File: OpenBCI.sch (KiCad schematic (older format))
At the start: 12 parts, among them U6 ADS1299

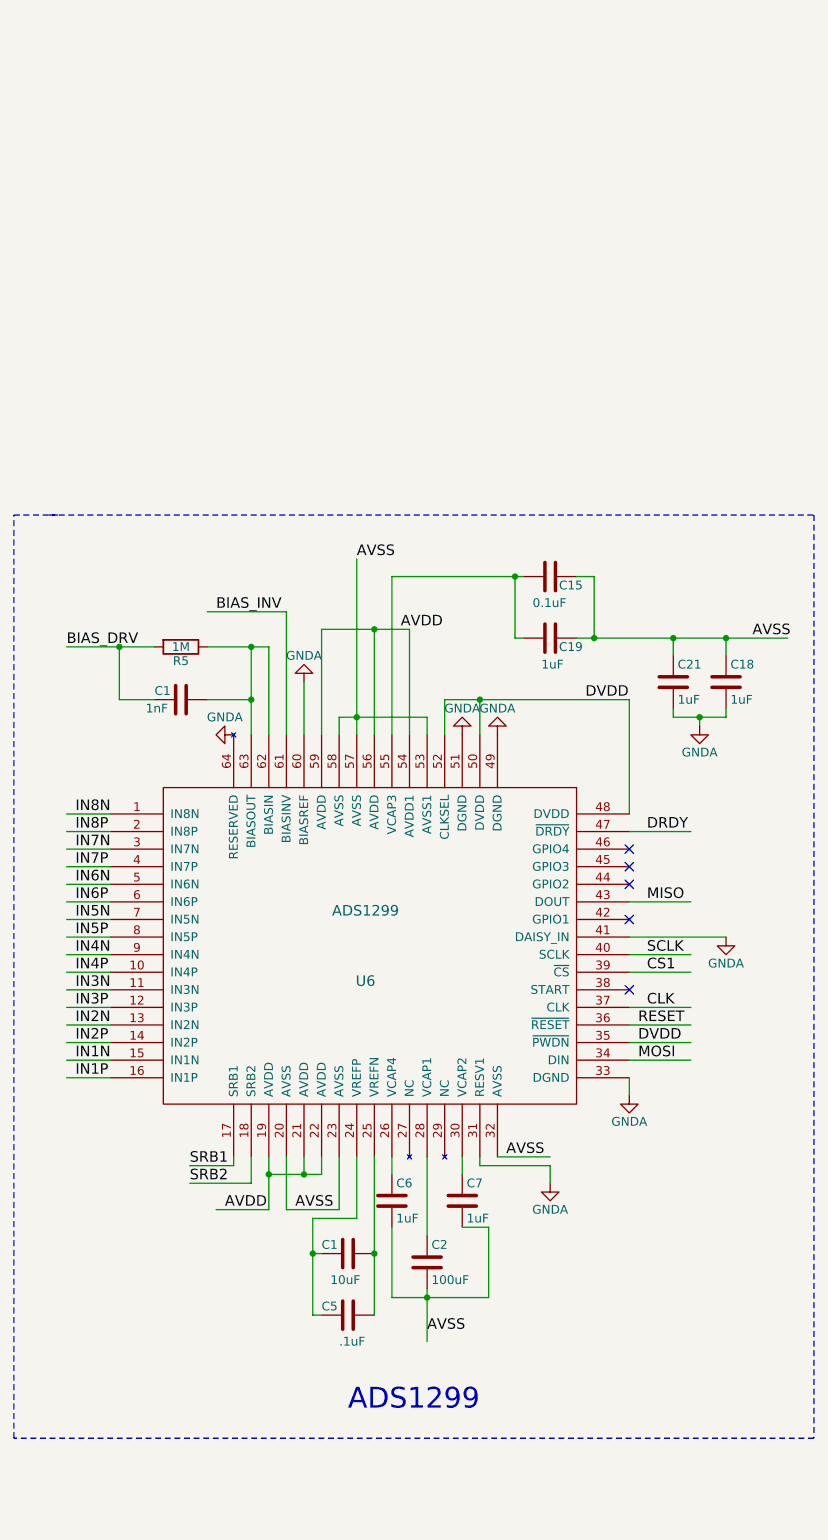
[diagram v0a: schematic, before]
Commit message: Chipkit pin breakout, input connector and daisy bus blocks added
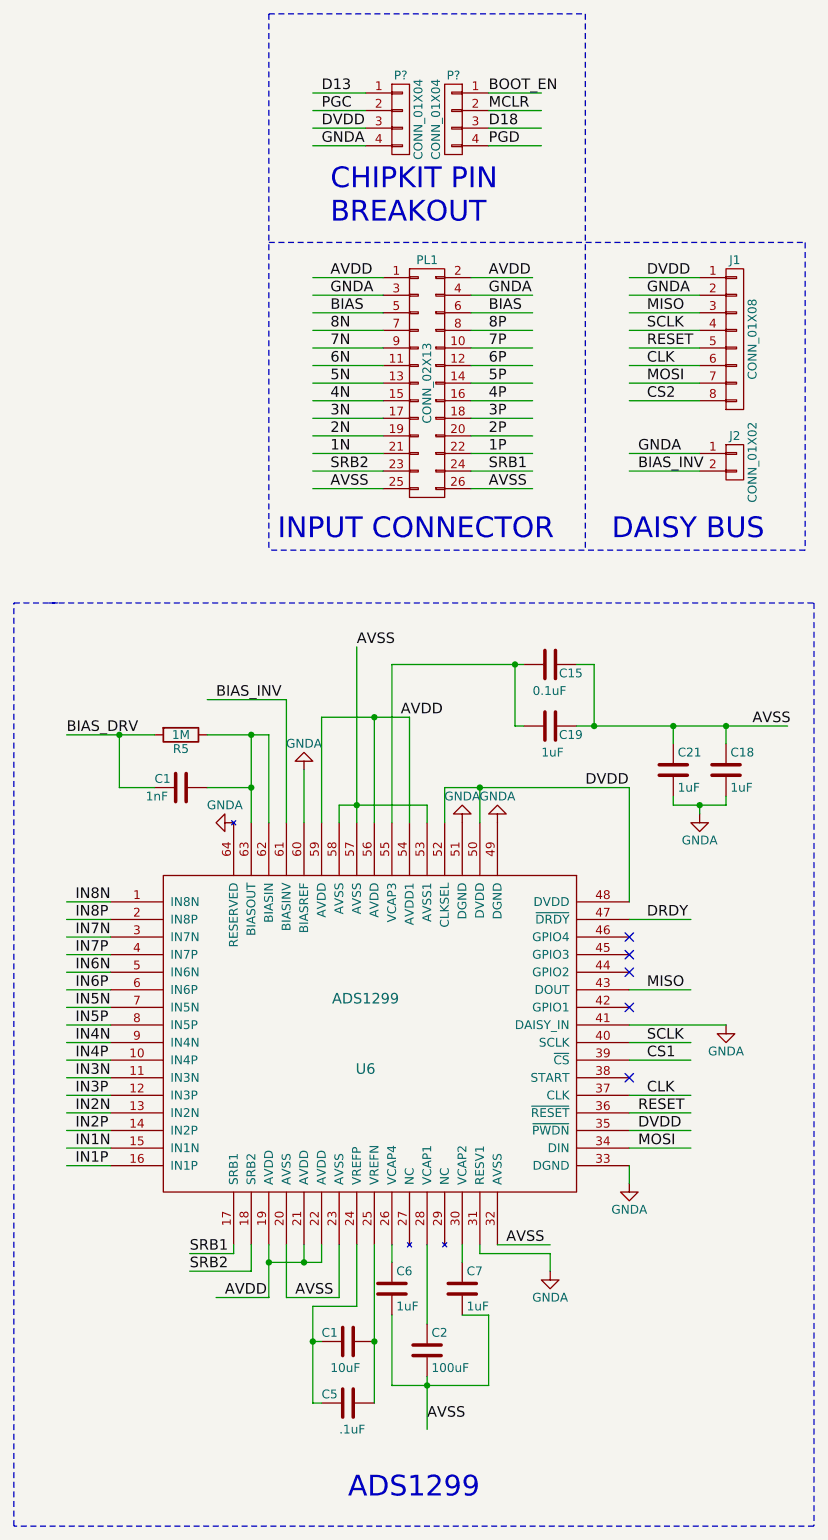
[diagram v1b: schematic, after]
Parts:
- added J1: CONN_01X08, symbol CONN_01X08
- added J2: CONN_01X02, symbol CONN_01X02
- added P? (x2): CONN_01X04, symbol CONN_01X04
- added PL1: CONN_02X13, symbol CONN_02X13
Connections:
- net labels added: 1N, 1P, 2N, 2P, 3N, 3P, 4N, 4P, 5N, 5P, 6N, 6P, 7N, 7P, 8N, 8P, BIAS, BOOT_EN, CS2, D13, D18, MCLR, PGC, PGD
- wire segments 91 -> 135
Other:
- note added: "CHIPKIT PIN\nBREAKOUT"
- note added: "DAISY BUS"
- note added: "INPUT CONNECTOR"
- moved on the sheet: C1, C15, C18, C19, C2, C21, C5, C6, C7, R5, U6

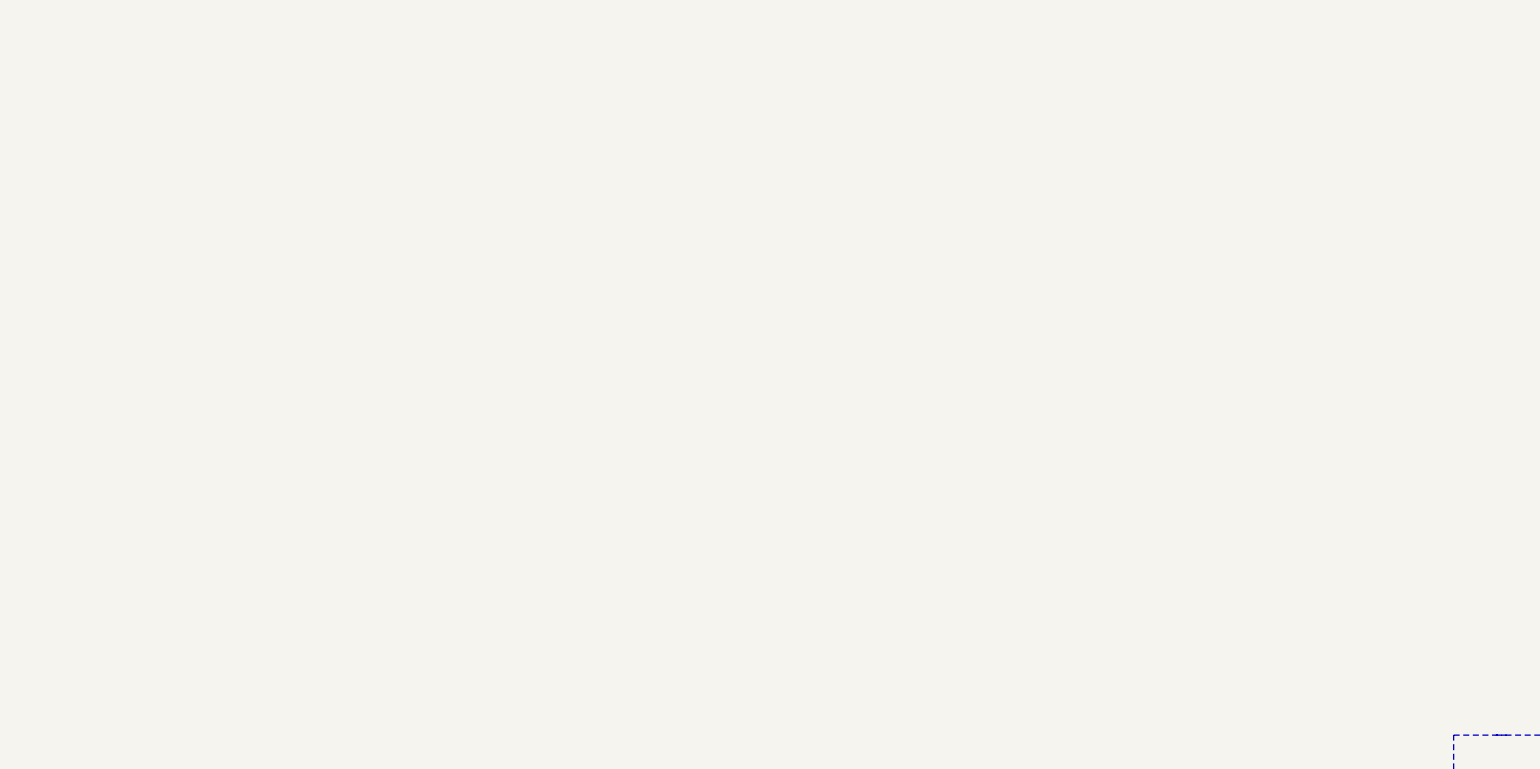
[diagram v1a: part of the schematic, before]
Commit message: +functional scheme and power supply draw
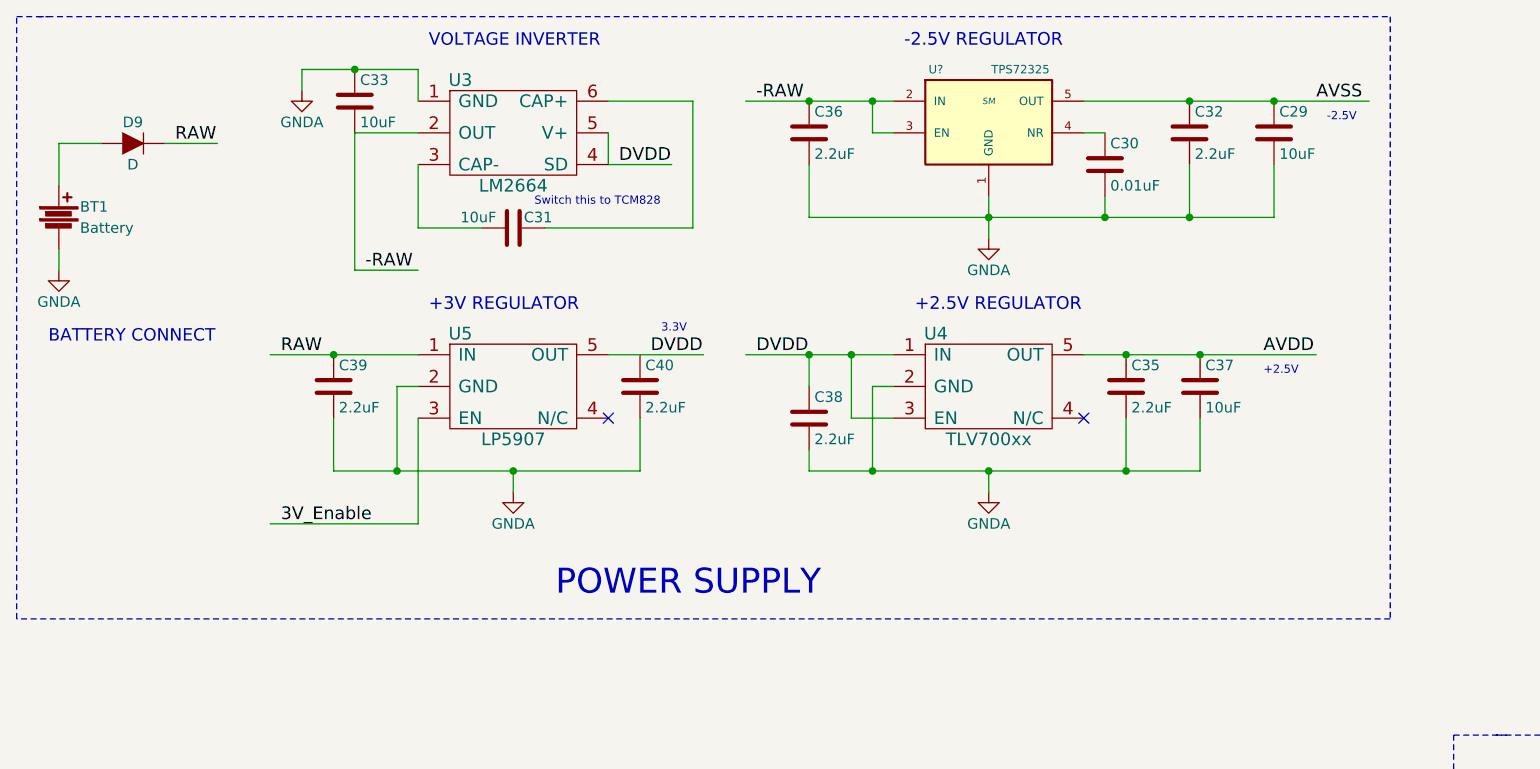
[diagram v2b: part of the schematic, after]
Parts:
- added BT1: Battery, symbol Battery
- added C29, C31, C33, C37: 10uF, symbol C
- added C30: 0.01uF, symbol C
- added C32, C35, C36, C38, C39, C40: 2.2uF, symbol C
- added D9: D, symbol D
- added U3: LM2664, symbol LM2664
- added U4: TLV700xx, symbol TLV700xx
- added U5: LP5907, symbol LP5907
- added U?: TPS72325, SM, symbol TPS72325
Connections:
- net labels added: -RAW, 3V_Enable, RAW
- wire segments 135 -> 186
- no-connect marks 5 -> 7
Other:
- note added: "+2.5V"
- note added: "+2.5V REGULATOR"
- note added: "+3V REGULATOR"
- note added: "-2.5V"
- note added: "-2.5V REGULATOR"
- note added: "3.3V"
- note added: "BATTERY CONNECT"
- note added: "POWER SUPPLY"
- note added: "Switch this to TCM828"
- note added: "VOLTAGE INVERTER"

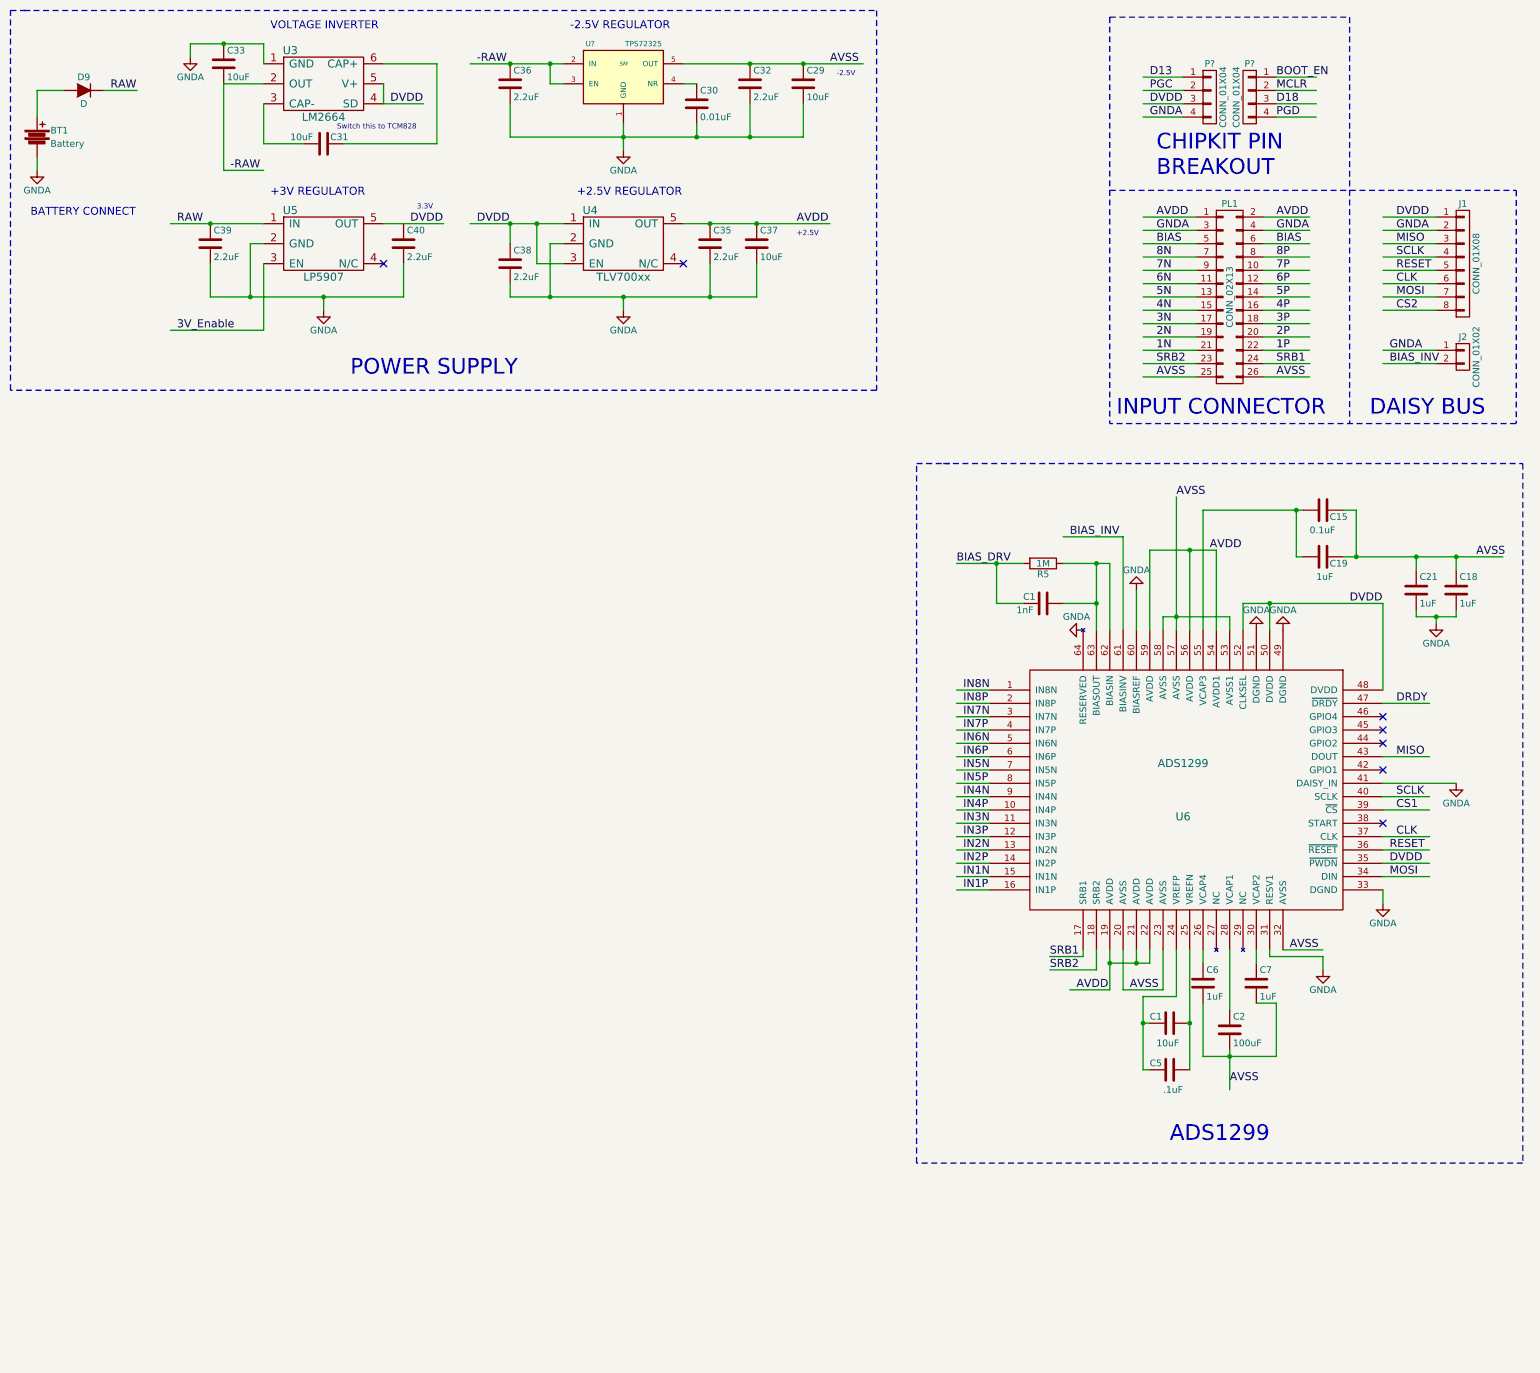
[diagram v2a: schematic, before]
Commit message: + ADS decoupling, SD CARD, ACCELEROMETER and imciner libraries
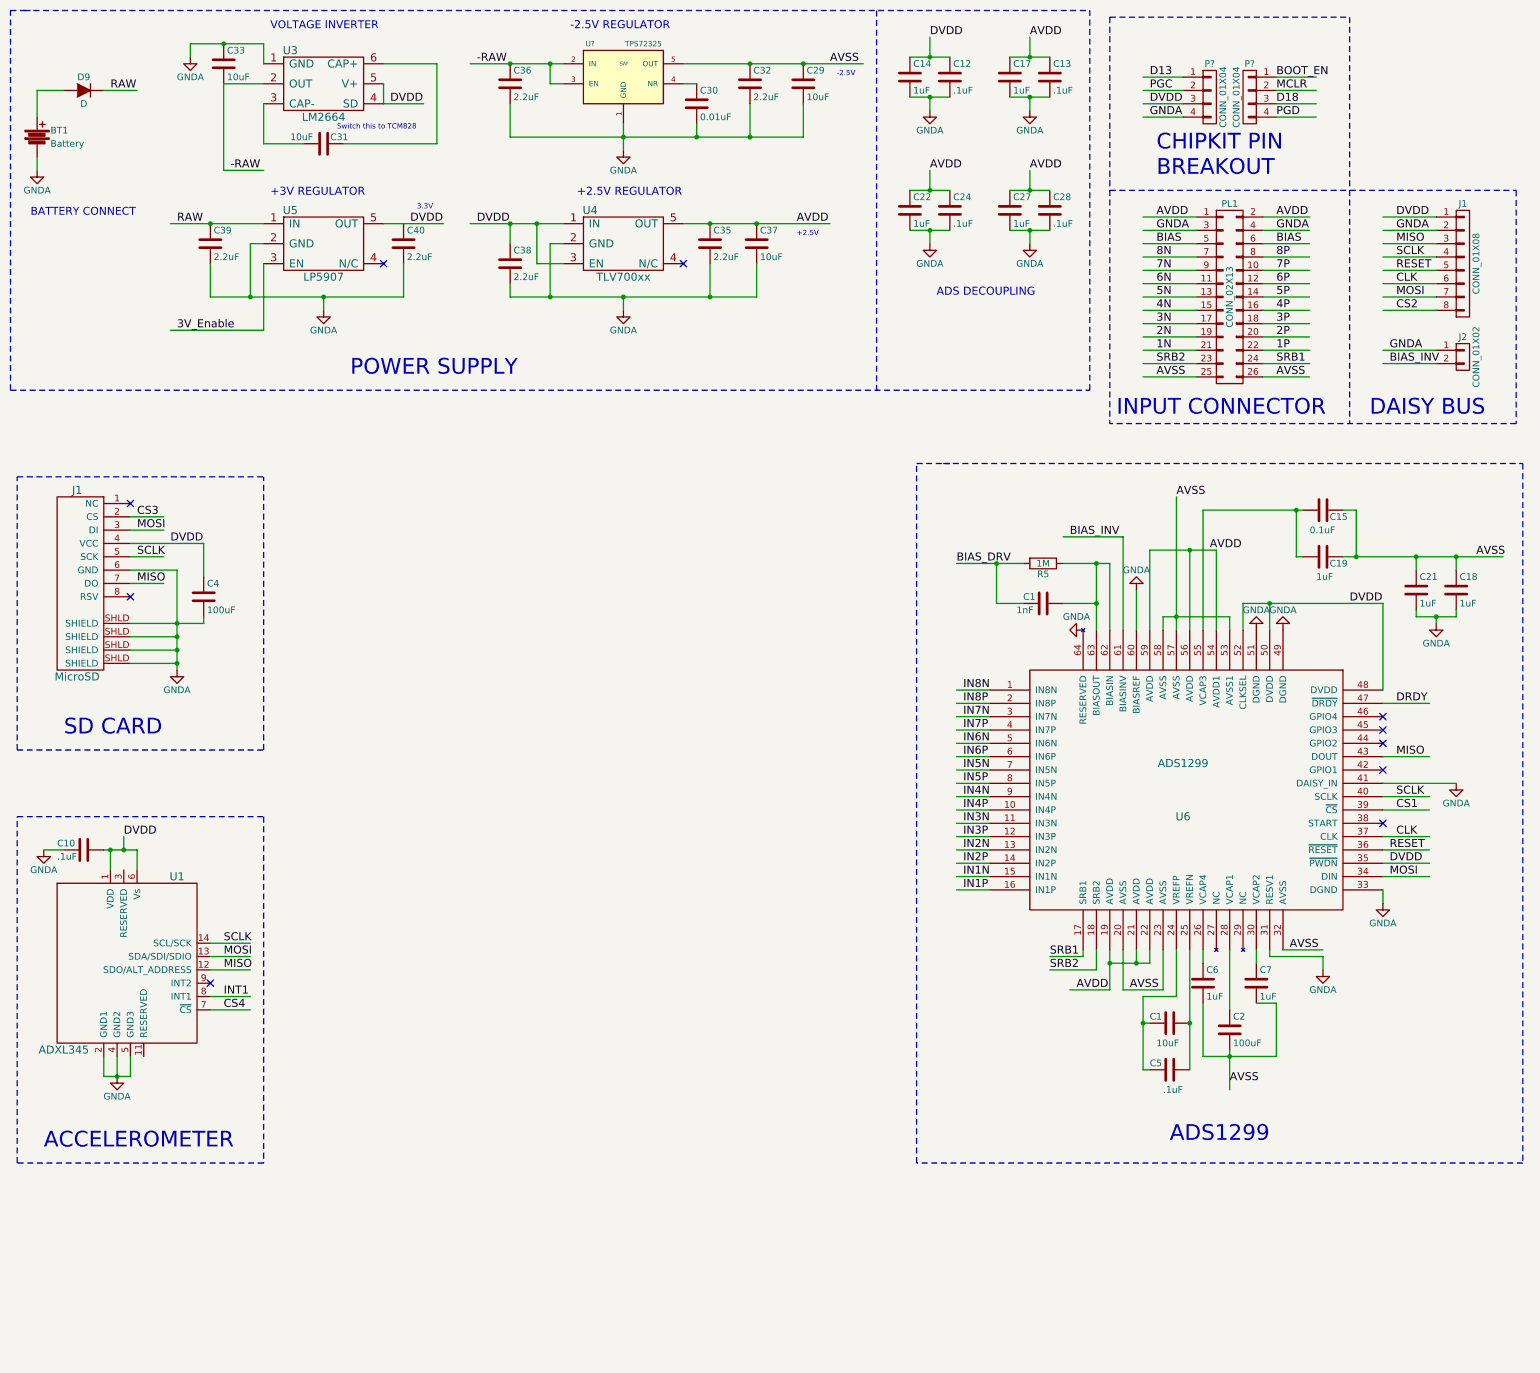
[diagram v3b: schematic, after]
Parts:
- added C10, C12, C13, C24, C28: .1uF, symbol C
- added C14, C17, C22, C27: 1uF, symbol C
- added C4: 100uF, symbol C
- added J1: MicroSD, symbol MicroSD
- added U1: ADXL345, symbol ADXL345
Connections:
- net labels added: CS3, CS4, INT1
- wire segments 186 -> 229
- no-connect marks 7 -> 10
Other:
- note added: "ACCELEROMETER"
- note added: "ADS DECOUPLING"
- note added: "SD CARD"
